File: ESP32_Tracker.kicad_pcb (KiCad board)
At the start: 4 copper layers, 60 x 75 mm, 75 parts, among them J1 USB_C_Receptacle_USB2.0_16P, J2 Conn_01x02_Socket, J3 Conn_01x03, J4 MSD-4-A, J5 Conn_01x07_Socket, SW1 SW_Push, SW2 SW_Push, SW3 SW_Push, SW4 SW_Push, SW5 SW_Push, U1 USBLC6-2SC6, U2 ESP32-S3-MINI-1, U3 MP2667, U4 XC6220B331MR-G, U5 LIS2MDL, U6 SAM-M10Q

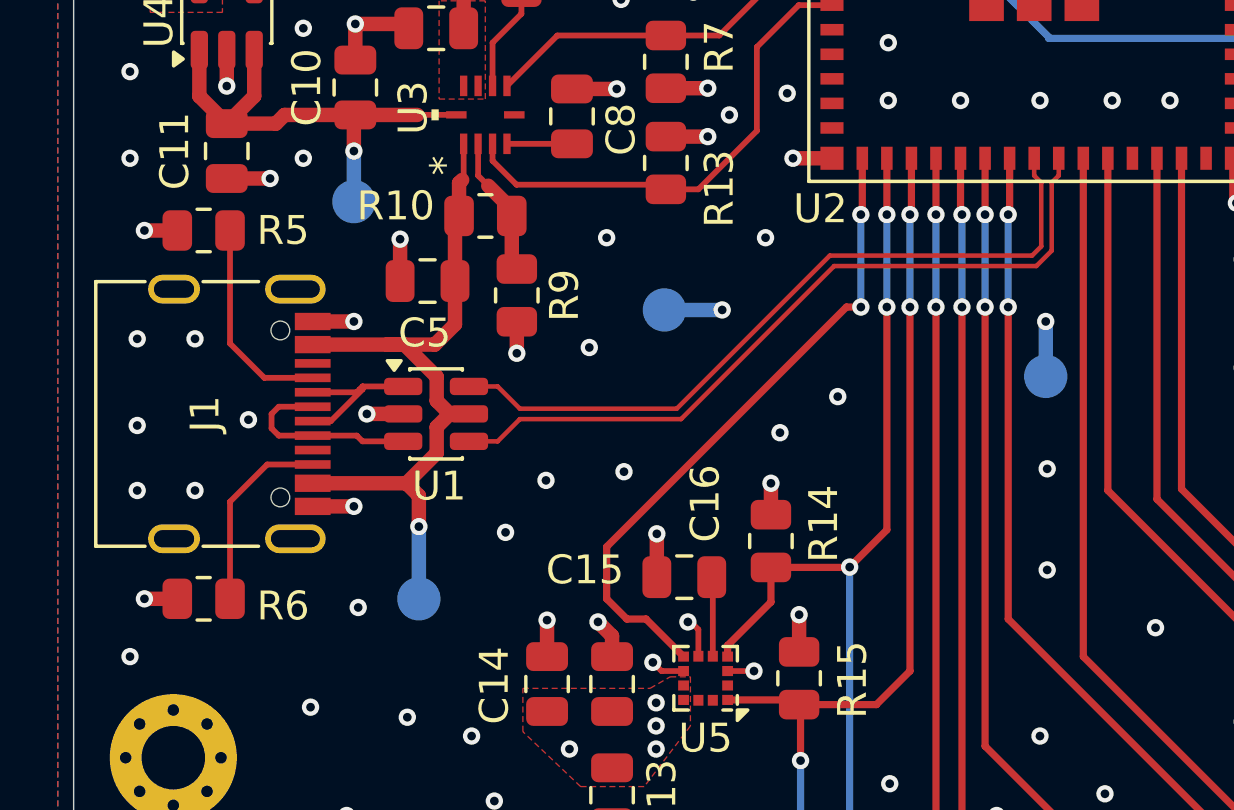
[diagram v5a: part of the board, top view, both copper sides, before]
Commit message: modified BOM
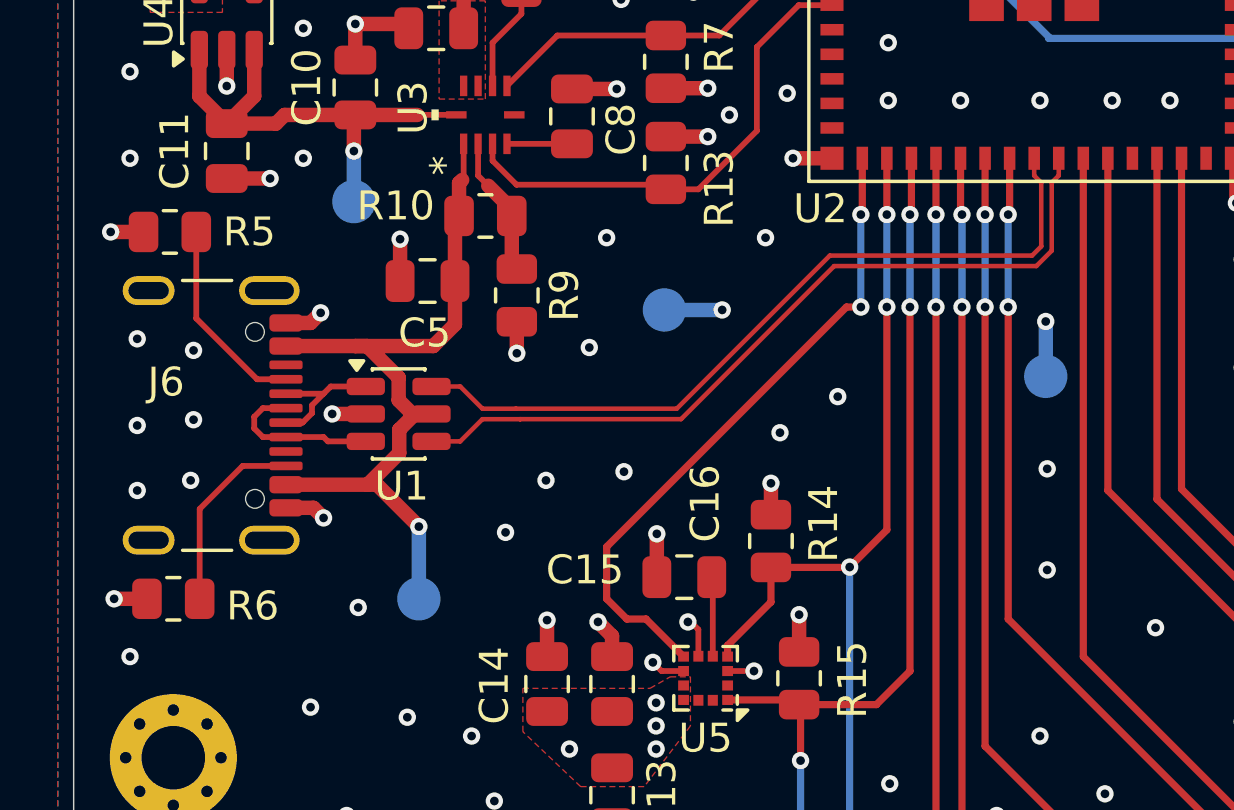
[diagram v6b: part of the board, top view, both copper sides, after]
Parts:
- removed J1: USB_C_Receptacle_USB2.0_16P, Connector_USB:USB_C_Receptacle_G-Switch_GT-USB-7010ASV
- added J6: USB_C_Receptacle_USB2.0_16P, Connector_USB:USB_C_Receptacle_GCT_USB4105-xx-A_16P_TopMnt_Horizontal, F.Cu at (117.7, 91.2)
- moved U1 1.30 mm to (125.3, 91.1)
- moved R5 1.17 mm to (117.4, 84.8)
- moved R6 1.05 mm to (117.5, 97.5)
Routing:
- net VBUS: track 26.4 -> 28.0 mm
- net /MCU/PWR/USB_D+: track 26.2 -> 27.5 mm
- net /MCU/PWR/USB_D-: track 25.6 -> 26.9 mm
- net Net-(J6-D+-PadA6): track 6.77 -> 5.67 mm
- net Net-(J6-D--PadA7): track 5.50 -> 4.74 mm

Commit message: modified BOM
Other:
- board text added: "Matthew Tubbin REV 1.0 1/16/2026 ECE-212"
- board text removed: "Matthew Tubbin REV 1.0 1/15/2026 ECE-212"
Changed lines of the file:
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@@
 		(tags "2.4 GHz Wi-Fi Bluetooth external antenna espressif  20*15.4mm")
 		(property "Reference" "U2"
-			(at -7.4 11.3 0)
+			(at -7.7 11.3 0)
 			(unlocked yes)
 			(layer "F.SilkS")
@@
 		)
 	)
-	(gr_text "Matthew Tubbin\nREV 1.0\n1/15/2026\nECE-212"
+	(gr_text "Matthew Tubbin\nREV 1.0\n1/16/2026\nECE-212"
 		(at 161.25 128 0)
 		(layer "F.SilkS")

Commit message: modified layout
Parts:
- SW1, SW3: footprint Button_Switch_SMD:SW_SPST_TS-1088-xR020 -> Button_Switch_SMD:SW_SPST_B3U-1000P
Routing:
- net GND: track 123.1 -> 121.4 mm
- net Net-(U2-EN): track 22.1 -> 22.7 mm
- net Net-(U2-IO0): track 31.3 -> 31.9 mm
